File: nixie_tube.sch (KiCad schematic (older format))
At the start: 15 parts, among them P1 CONN_01X02, Q1 MPSA92, Q2 IRF740, U1 MC34063

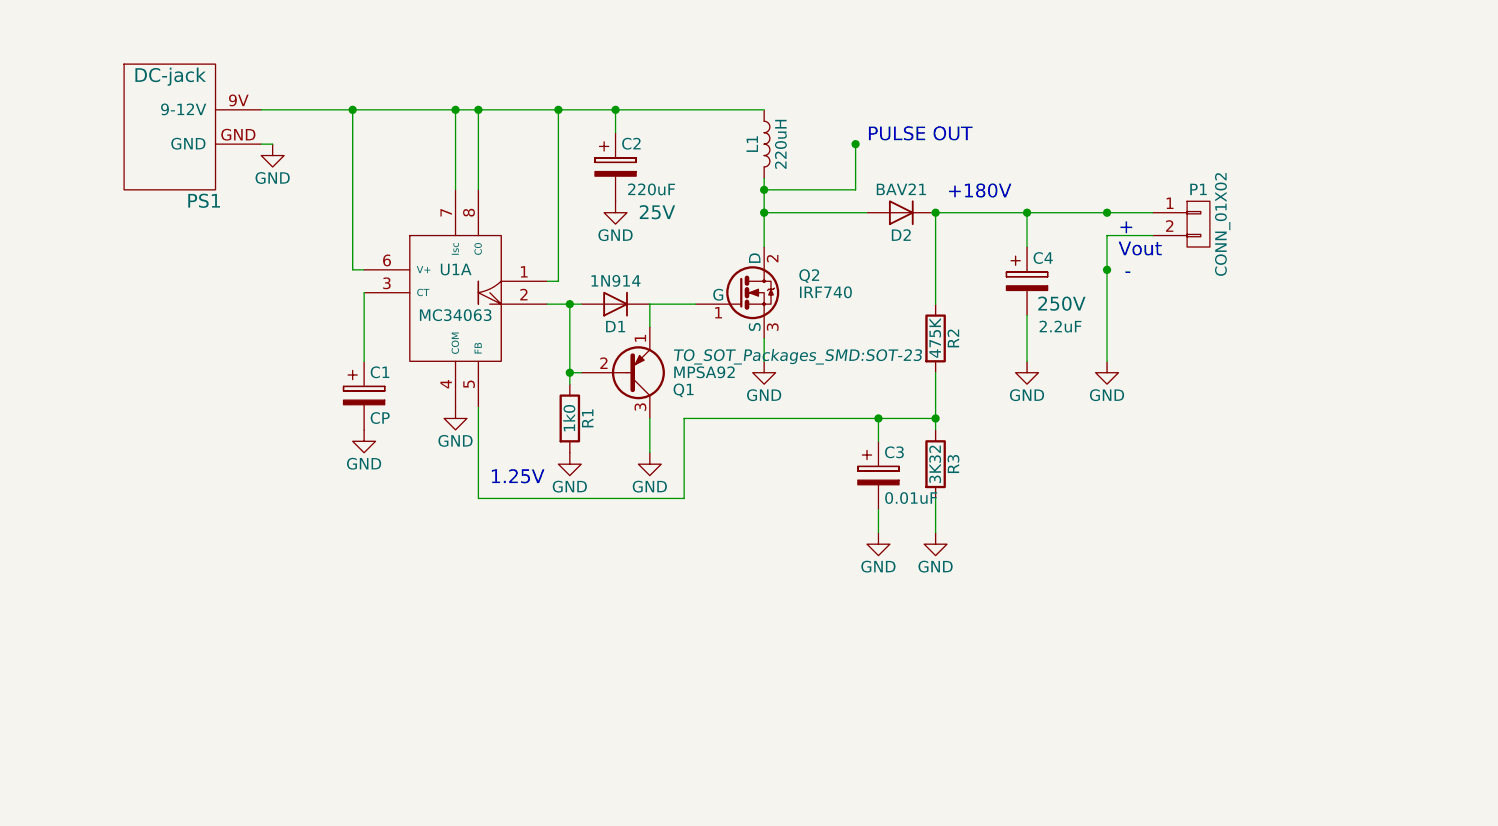
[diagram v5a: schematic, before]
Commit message: added 220uF 35V smd footprint
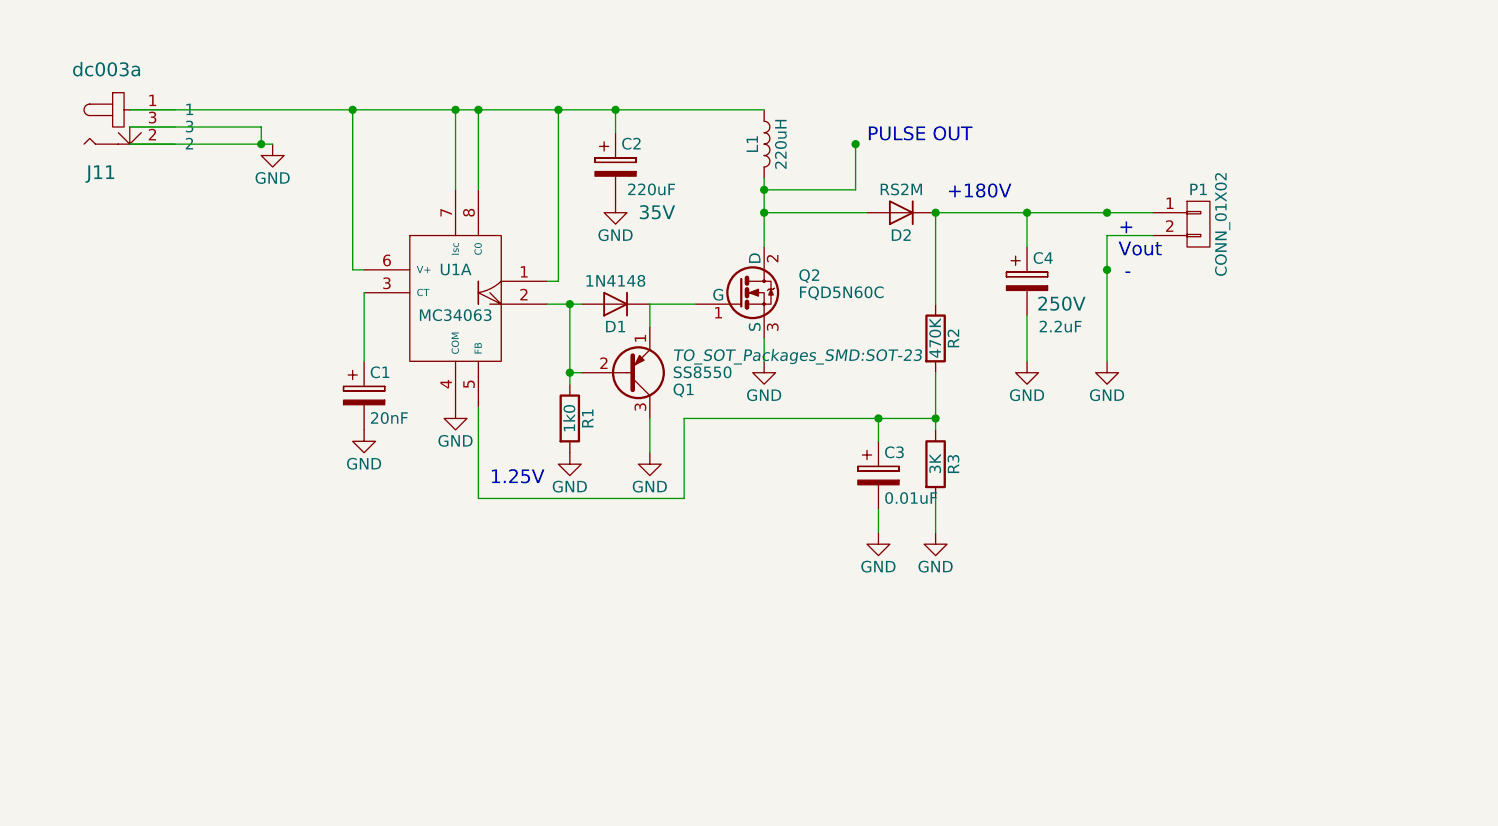
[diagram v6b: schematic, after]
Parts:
- removed PS1: DC-jack, symbol DC-jack
- added J11: dc003a, nixie-tube-fp:dc005a, symbol dc003a
- C1: value CP -> 20nF
- C2: footprint Capacitors_SMD:C_0603_HandSoldering -> nixie-tube-fp:220uF-35V-smd; voltage 25V -> 35V
- D1: value 1N914 -> 1N4148; footprint Diodes_SMD:DO-214AB_Handsoldering -> Diodes_SMD:D_SOD-123
- D2: value BAV21 -> RS2M; footprint Diodes_SMD:DO-214AB_Handsoldering -> Diodes_SMD:D_SMA
- Q1: value MPSA92 -> SS8550
- Q2: value IRF740 -> FQD5N60C
- R2: value 475K -> 470K
- R3: value 3K32 -> 3K
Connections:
- net GND: now also J11.2, J11.3
- net at C2.1, L1.1, U1.1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: now also J11.1
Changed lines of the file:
@@
 F 0 "C2" H 4175 2550 50  0000 L CNN
 F 1 "220uF" H 4200 2350 50  0000 L CNN
-F 2 "Capacitors_SMD:C_0603_HandSoldering" H 4188 2300 50  0001 C CNN
+F 2 "nixie-tube-fp:220uF-35V-smd" H 4188 2300 50  0001 C CNN
 F 3 "" H 4150 2450 50  0000 C CNN
-F 4 "25V" H 4250 2250 60  0000 L CNN "voltage"
+F 4 "35V" H 4250 2250 60  0000 L CNN "voltage"
 	1    4150 2450
 	1    0    0    -1
@@
 P 5400 2650
 F 0 "D2" H 5400 2750 50  0000 C CNN
-F 1 "BAV21" H 5400 2550 50  0000 C CNN
-F 2 "Diodes_SMD:DO-214AB_Handsoldering" H 5400 2650 50  0001 C CNN
+F 1 "RS2M" H 5400 2550 50  0000 C CNN
+F 2 "Diodes_SMD:D_SMA" H 5400 2650 50  0001 C CNN
 F 3 "" H 5400 2650 50  0000 C CNN
 	1    5400 2650
@@
 P 5550 3200
 F 0 "R2" V 5630 3200 50  0000 C CNN
-F 1 "475K" V 5550 3200 50  0000 C CNN
+F 1 "470K" V 5550 3200 50  0000 C CNN
 F 2 "Resistors_SMD:R_0603_HandSoldering" V 5480 3200 50  0001 C CNN
 F 3 "" H 5550 3200 50  0000 C CNN
@@
 P 5550 3750
 F 0 "R3" V 5630 3750 50  0000 C CNN
-F 1 "3K32" V 5550 3750 50  0000 C CNN
+F 1 "3K" V 5550 3750 50  0000 C CNN
 F 2 "Resistors_SMD:R_0603_HandSoldering" V 5480 3750 50  0001 C CNN
 F 3 "" H 5550 3750 50  0000 C CNN
@@
 P 4150 3050
 F 0 "D1" H 4150 3150 50  0000 C CNN
-F 1 "1N914" H 4150 2950 50  0000 C CNN
-F 2 "Diodes_SMD:DO-214AB_Handsoldering" H 4150 3050 50  0001 C CNN
+F 1 "1N4148" H 4150 2950 50  0000 C CNN
+F 2 "Diodes_SMD:D_SOD-123" H 4150 3050 50  0001 C CNN
 F 3 "" H 4150 3050 50  0000 C CNN
 	1    4150 3050
@@
 P 4200 3350
 F 0 "Q1" H 4400 3425 50  0000 L CNN
-F 1 "MPSA92" H 4400 3350 50  0000 L CNN
+F 1 "SS8550" H 4400 3350 50  0000 L CNN
 F 2 "TO_SOT_Packages_SMD:SOT-23" H 4400 3275 50  0000 L CIN
 F 3 "" H 4200 3350 50  0000 L CNN
@@
 P 3050 3450
 F 0 "C1" H 3075 3550 50  0000 L CNN
-F 1 "CP" H 3075 3350 50  0000 L CNN
+F 1 "20nF" H 3075 3350 50  0000 L CNN
 F 2 "Capacitors_SMD:C_0603_HandSoldering" H 3088 3300 50  0001 C CNN
 F 3 "" H 3050 3450 50  0000 C CNN
@@
 P 4700 3000
 F 0 "Q2" H 4950 3075 50  0000 L CNN
-F 1 "IRF740" H 4950 3000 50  0000 L CNN
+F 1 "FQD5N60C" H 4950 3000 50  0000 L CNN
 F 2 "TO_SOT_Packages_SMD:TO-252-2Lead" H 4950 2925 50  0001 L CIN
 F 3 "" H 4700 3000 50  0000 L CNN
@@
 $EndComp
 $Comp
-L DC-jack PS1
-U 1 1 59D9D39C
-P 2600 2300
-F 0 "PS1" H 2350 2000 60  0000 C CNN
-F 1 "DC-jack" H 2200 2550 60  0000 C CNN
-F 2 "" H 2600 2300 60  0001 C CNN
-F 3 "" H 2600 2300 60  0001 C CNN
-	1    2600 2300
-	1    0    0    -1
-$EndComp
-Wire Wire Line
-	2600 2200 4800 2200
-Wire Wire Line
-	3450 2200 3450 2550
-Connection ~ 3450 2200
-Wire Wire Line
-	3850 2950 3900 2950
-Wire Wire Line
-	3900 2950 3900 2200
-Connection ~ 3550 2200
-Wire Wire Line
-	4150 2200 4150 2300
-Connection ~ 3900 2200
-Connection ~ 4150 2200
-Wire Wire Line
-	5550 2650 5550 3050
-Wire Wire Line
-	3550 3900 4450 3900
-Wire Wire Line
-	3550 3500 3550 3900
-Wire Wire Line
-	3850 3050 4000 3050
-Wire Wire Line
-	4300 3050 4300 3150
-Wire Wire Line
-	3950 3050 3950 3400
-Wire Wire Line
-	3950 3350 4000 3350
-Connection ~ 3950 3050
-Connection ~ 3950 3350
-Wire Wire Line
-	3050 3000 3050 3300
-Wire Wire Line
-	3000 2200 3000 2900
-Wire Wire Line
-	3000 2900 3050 2900
-Connection ~ 3000 2200
-Wire Wire Line
-	4800 3200 4800 3300
-Wire Wire Line
-	4300 3050 4500 3050
-Wire Wire Line
-	4800 2500 4800 2800
-Wire Wire Line
-	4800 2650 5250 2650
-Connection ~ 4800 2650
-Wire Wire Line
-	4800 2550 5200 2550
-Wire Wire Line
-	5200 2550 5200 2350
-Connection ~ 4800 2550
-Connection ~ 5200 2350
-Wire Wire Line
-	4450 3900 4450 3550
-Wire Wire Line
-	4450 3550 5550 3550
-Wire Wire Line
-	5550 3350 5550 3600
-Connection ~ 5550 3550
-Wire Wire Line
-	5300 3650 5300 3550
-Connection ~ 5300 3550
-Wire Wire Line
-	5300 3950 5300 4050
-Wire Wire Line
-	5550 2650 6500 2650
-Wire Wire Line
-	5950 2650 5950 2800
-Wire Wire Line
-	5950 3300 5950 3100
-Connection ~ 5950 2650
-Connection ~ 6300 2650
-Connection ~ 6300 2900
-Wire Wire Line
-	6300 2750 6300 3300
-Connection ~ 5550 2650
-Wire Wire Line
-	4300 3550 4300 3700
-Wire Wire Line
-	3550 2200 3550 2550
-Wire Wire Line
-	5550 4050 5550 3900
-$Comp
 L GND #PWR011
 U 1 1 59D51046
@@
 	1    0    0    -1
 $EndComp
-Wire Wire Line
-	2600 2350 2650 2350
 $Comp
 L CONN_01X02 P1
@@
 	1    0    0    -1
 $EndComp
+$Comp
+L dc003a J11
+U 1 1 59DD8DA0
+P 1900 2225
+F 0 "J11" H 1900 1975 60  0000 C CNN
+F 1 "dc003a" H 1925 2425 60  0000 C CNN
+F 2 "nixie-tube-fp:dc005a" H 1900 2225 60  0001 C CNN
+F 3 "" H 1900 2225 60  0001 C CNN
+	1    1900 2225
+	1    0    0    -1
+$EndComp
+Wire Wire Line
+	3450 2200 3450 2550
+Connection ~ 3450 2200
+Wire Wire Line
+	3850 2950 3900 2950
+Wire Wire Line
+	3900 2950 3900 2200
+Connection ~ 3550 2200
+Wire Wire Line
+	4150 2200 4150 2300
+Connection ~ 3900 2200
+Connection ~ 4150 2200
+Wire Wire Line
+	5550 2650 5550 3050
+Wire Wire Line
+	3550 3900 4450 3900
+Wire Wire Line
+	3550 3500 3550 3900
+Wire Wire Line
+	3850 3050 4000 3050
+Wire Wire Line
+	4300 3050 4300 3150
+Wire Wire Line
+	3950 3050 3950 3400
+Wire Wire Line
+	3950 3350 4000 3350
+Connection ~ 3950 3050
+Connection ~ 3950 3350
+Wire Wire Line
+	3050 3000 3050 3300
+Wire Wire Line
+	3000 2200 3000 2900
+Wire Wire Line
+	3000 2900 3050 2900
+Connection ~ 3000 2200
+Wire Wire Line
+	4800 3200 4800 3300
+Wire Wire Line
+	4300 3050 4500 3050
+Wire Wire Line
+	4800 2500 4800 2800
+Wire Wire Line
+	4800 2650 5250 2650
+Connection ~ 4800 2650
+Wire Wire Line
+	4800 2550 5200 2550
+Wire Wire Line
+	5200 2550 5200 2350
+Connection ~ 4800 2550
+Connection ~ 5200 2350
+Wire Wire Line
+	4450 3900 4450 3550
+Wire Wire Line
+	4450 3550 5550 3550
+Wire Wire Line
+	5550 3350 5550 3600
+Connection ~ 5550 3550
+Wire Wire Line
+	5300 3650 5300 3550
+Connection ~ 5300 3550
+Wire Wire Line
+	5300 3950 5300 4050
+Wire Wire Line
+	5550 2650 6500 2650
+Wire Wire Line
+	5950 2650 5950 2800
+Wire Wire Line
+	5950 3300 5950 3100
+Connection ~ 5950 2650
+Connection ~ 6300 2650
+Connection ~ 6300 2900
+Wire Wire Line
+	6300 2750 6300 3300
+Connection ~ 5550 2650
+Wire Wire Line
+	4300 3550 4300 3700
+Wire Wire Line
+	3550 2200 3550 2550
+Wire Wire Line
+	5550 4050 5550 3900
+Wire Wire Line
+	2025 2350 2650 2350
 Wire Wire Line
 	6300 2750 6500 2750
+Wire Wire Line
+	2025 2275 2600 2275
+Wire Wire Line
+	2600 2275 2600 2350
+Connection ~ 2600 2350
+Wire Wire Line
+	2025 2200 4800 2200
 $EndSCHEMATC

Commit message: added 5 female and male pin headers at schematic
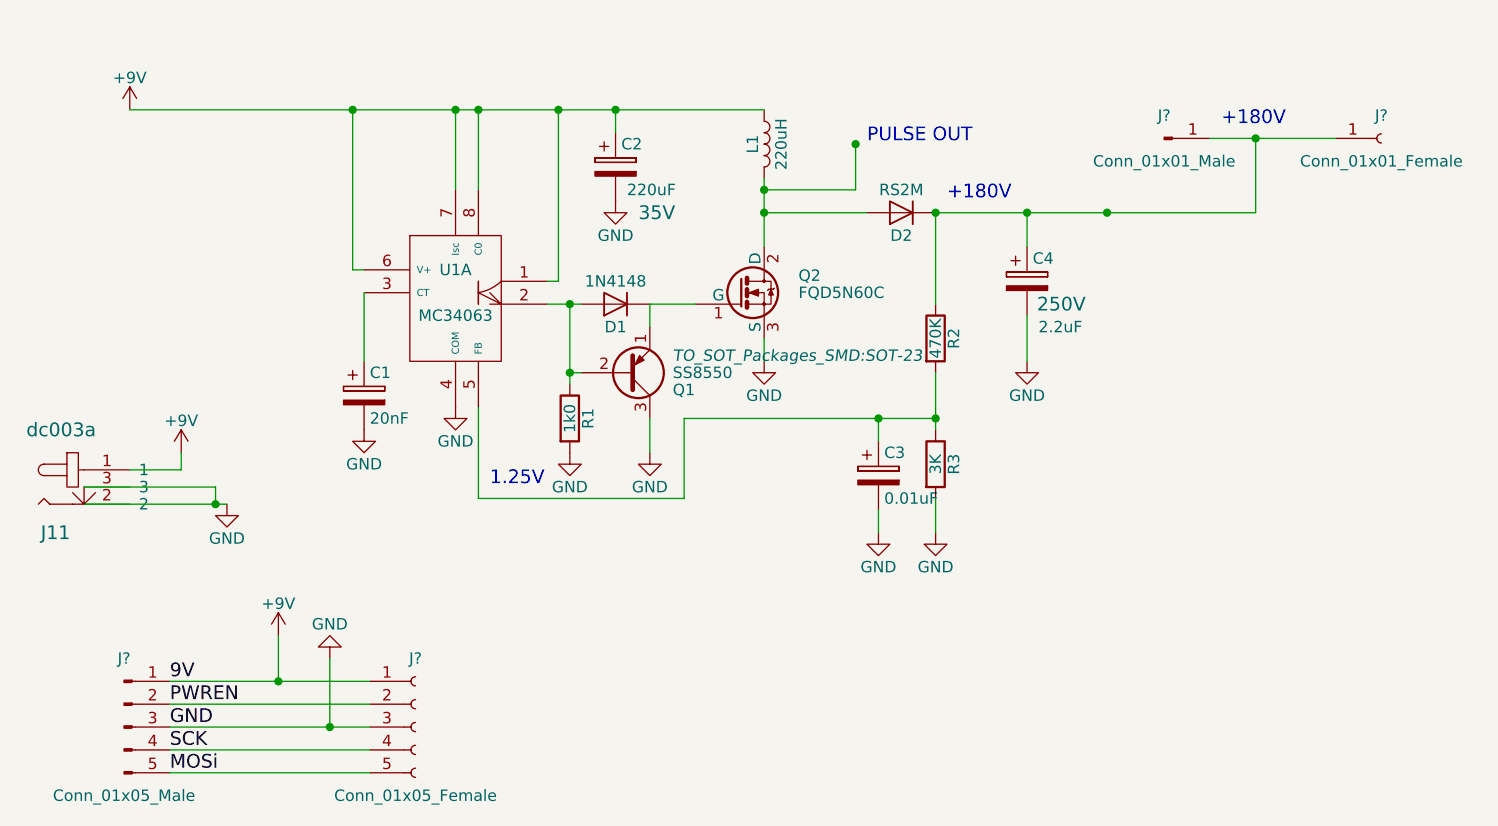
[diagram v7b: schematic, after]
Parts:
- removed P1: CONN_01X02, Pin_Headers:Pin_Header_Angled_1x02, symbol CONN_01X02
- added J?: Conn_01x01_Female, symbol Conn_01x01_Female
- added J?: Conn_01x01_Male, symbol Conn_01x01_Male
- added J?: Conn_01x05_Female, symbol Conn_01x05_Female
- added J?: Conn_01x05_Male, symbol Conn_01x05_Male
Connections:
- net GND: now also J?.3 (Pin_3), J?.3 (Pin_3)
- net +9V: now reaches C2.1, L1.1, U1.1, U1.6 (V+), U1.7 (Isc), U1.8 (C0)
- net +9V: now also J?.1 (Pin_1), J?.1 (Pin_1); no longer J11.1
- net at C4.1, D2.1 (K), R2.1: now also J?.1 (Pin_1), J?.1 (Pin_1)
- new net MOSi: J?.5 (Pin_5), J?.5 (Pin_5)
- new net PWREN: J?.2 (Pin_2), J?.2 (Pin_2)
- new net SCK: J?.4 (Pin_4), J?.4 (Pin_4)
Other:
- note removed: "+\nVout\n -"
- moved on the sheet: J11
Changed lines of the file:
@@
 	1    0    0    -1
 $EndComp
-$Comp
-L GND #PWR07
-U 1 1 59D52602
-P 6300 3300
-F 0 "#PWR07" H 6300 3050 50  0001 C CNN
-F 1 "GND" H 6300 3150 50  0000 C CNN
-F 2 "" H 6300 3300 50  0000 C CNN
-F 3 "" H 6300 3300 50  0000 C CNN
-	1    6300 3300
-	1    0    0    -1
-$EndComp
-Text Notes 6350 2950 0    60   ~ 0
- +\nVout\n -
 Text Notes 3600 3850 0    60   ~ 0
 1.25V
@@
 L GND #PWR011
 U 1 1 59D51046
-P 2650 2350
-F 0 "#PWR011" H 2650 2100 50  0001 C CNN
-F 1 "GND" H 2650 2200 50  0000 C CNN
-F 2 "" H 2650 2350 50  0000 C CNN
-F 3 "" H 2650 2350 50  0000 C CNN
-	1    2650 2350
-	1    0    0    -1
-$EndComp
-$Comp
-L CONN_01X02 P1
-U 1 1 59DBC560
-P 6700 2700
-F 0 "P1" H 6700 2850 50  0000 C CNN
-F 1 "CONN_01X02" V 6800 2700 50  0000 C CNN
-F 2 "Pin_Headers:Pin_Header_Angled_1x02" H 6700 2700 50  0001 C CNN
-F 3 "" H 6700 2700 50  0000 C CNN
-	1    6700 2700
+P 2450 3925
+F 0 "#PWR011" H 2450 3675 50  0001 C CNN
+F 1 "GND" H 2450 3775 50  0000 C CNN
+F 2 "" H 2450 3925 50  0000 C CNN
+F 3 "" H 2450 3925 50  0000 C CNN
+	1    2450 3925
 	1    0    0    -1
 $EndComp
@@
 L dc003a J11
 U 1 1 59DD8DA0
-P 1900 2225
-F 0 "J11" H 1900 1975 60  0000 C CNN
-F 1 "dc003a" H 1925 2425 60  0000 C CNN
-F 2 "nixie-tube-fp:dc005a" H 1900 2225 60  0001 C CNN
-F 3 "" H 1900 2225 60  0001 C CNN
-	1    1900 2225
+P 1700 3800
+F 0 "J11" H 1700 3550 60  0000 C CNN
+F 1 "dc003a" H 1725 4000 60  0000 C CNN
+F 2 "nixie-tube-fp:dc005a" H 1700 3800 60  0001 C CNN
+F 3 "" H 1700 3800 60  0001 C CNN
+	1    1700 3800
+	1    0    0    -1
+$EndComp
+$Comp
+L Conn_01x01_Female J?
+U 1 1 59E5D8C8
+P 7500 2325
+F 0 "J?" H 7500 2425 50  0000 C CNN
+F 1 "Conn_01x01_Female" H 7500 2225 50  0000 C CNN
+F 2 "" H 7500 2325 50  0001 C CNN
+F 3 "" H 7500 2325 50  0001 C CNN
+	1    7500 2325
+	1    0    0    -1
+$EndComp
+$Comp
+L Conn_01x01_Male J?
+U 1 1 59E5D935
+P 6550 2325
+F 0 "J?" H 6550 2425 50  0000 C CNN
+F 1 "Conn_01x01_Male" H 6550 2225 50  0000 C CNN
+F 2 "" H 6550 2325 50  0001 C CNN
+F 3 "" H 6550 2325 50  0001 C CNN
+	1    6550 2325
+	1    0    0    -1
+$EndComp
+$Comp
+L Conn_01x05_Female J?
+U 1 1 59E5DA12
+P 3275 4900
+F 0 "J?" H 3275 5200 50  0000 C CNN
+F 1 "Conn_01x05_Female" H 3275 4600 50  0000 C CNN
+F 2 "" H 3275 4900 50  0001 C CNN
+F 3 "" H 3275 4900 50  0001 C CNN
+	1    3275 4900
+	1    0    0    -1
+$EndComp
+$Comp
+L Conn_01x05_Male J?
+U 1 1 59E5DABD
+P 2000 4900
+F 0 "J?" H 2000 5200 50  0000 C CNN
+F 1 "Conn_01x05_Male" H 2000 4600 50  0000 C CNN
+F 2 "" H 2000 4900 50  0001 C CNN
+F 3 "" H 2000 4900 50  0001 C CNN
+	1    2000 4900
+	1    0    0    -1
+$EndComp
+Text Label 2200 4700 0    60   ~ 0
+9V
+Text Label 2200 4800 0    60   ~ 0
+PWREN
+Text Label 2200 4900 0    60   ~ 0
+GND
+Text Label 2200 5000 0    60   ~ 0
+SCK
+Text Label 2200 5100 0    60   ~ 0
+MOSi
+$Comp
+L +9V #PWR?
+U 1 1 59E5E8EF
+P 2250 3700
+F 0 "#PWR?" H 2250 3550 50  0001 C CNN
+F 1 "+9V" H 2250 3840 50  0000 C CNN
+F 2 "" H 2250 3700 50  0001 C CNN
+F 3 "" H 2250 3700 50  0001 C CNN
+	1    2250 3700
 	1    0    0    -1
 $EndComp
@@
 	5300 3950 5300 4050
 Wire Wire Line
-	5550 2650 6500 2650
+	5550 2650 6950 2650
 Wire Wire Line
 	5950 2650 5950 2800
@@
 Connection ~ 5950 2650
 Connection ~ 6300 2650
-Connection ~ 6300 2900
-Wire Wire Line
-	6300 2750 6300 3300
 Connection ~ 5550 2650
 Wire Wire Line
@@
 	5550 4050 5550 3900
 Wire Wire Line
-	2025 2350 2650 2350
-Wire Wire Line
-	6300 2750 6500 2750
-Wire Wire Line
-	2025 2275 2600 2275
-Wire Wire Line
-	2600 2275 2600 2350
-Connection ~ 2600 2350
+	1825 3925 2450 3925
+Wire Wire Line
+	1825 3850 2400 3850
+Wire Wire Line
+	2400 3850 2400 3925
+Connection ~ 2400 3925
 Wire Wire Line
 	2025 2200 4800 2200
+Wire Wire Line
+	2200 4700 3075 4700
+Wire Wire Line
+	3075 4800 2200 4800
+Wire Wire Line
+	2200 4900 3075 4900
+Wire Wire Line
+	3075 5000 2200 5000
+Wire Wire Line
+	2200 5100 3075 5100
+Wire Wire Line
+	2025 3775 2250 3775
+Wire Wire Line
+	2250 3775 2250 3700
+$Comp
+L +9V #PWR?
+U 1 1 59E5EBB2
+P 2025 2200
+F 0 "#PWR?" H 2025 2050 50  0001 C CNN
+F 1 "+9V" H 2025 2340 50  0000 C CNN
+F 2 "" H 2025 2200 50  0001 C CNN
+F 3 "" H 2025 2200 50  0001 C CNN
+	1    2025 2200
+	1    0    0    -1
+$EndComp
+$Comp
+L +9V #PWR?
+U 1 1 59E5EF02
+P 2675 4500
+F 0 "#PWR?" H 2675 4350 50  0001 C CNN
+F 1 "+9V" H 2675 4640 50  0000 C CNN
+F 2 "" H 2675 4500 50  0001 C CNN
+F 3 "" H 2675 4500 50  0001 C CNN
+	1    2675 4500
+	1    0    0    -1
+$EndComp
+Wire Wire Line
+	2675 4500 2675 4700
+Connection ~ 2675 4700
+$Comp
+L GND #PWR?
+U 1 1 59E5EFC2
+P 2900 4600
+F 0 "#PWR?" H 2900 4350 50  0001 C CNN
+F 1 "GND" H 2900 4450 50  0000 C CNN
+F 2 "" H 2900 4600 50  0001 C CNN
+F 3 "" H 2900 4600 50  0001 C CNN
+	1    2900 4600
+	-1   0    0    1
+$EndComp
+Wire Wire Line
+	2900 4900 2900 4600
+Connection ~ 2900 4900
+Wire Wire Line
+	6950 2650 6950 2325
+Wire Wire Line
+	6750 2325 7300 2325
+Connection ~ 6950 2325
+Text Notes 6800 2275 0    60   ~ 0
++180V
 $EndSCHEMATC
